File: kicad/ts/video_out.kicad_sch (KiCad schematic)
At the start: 36 parts, among them T1 PN2222A, X5 74LS157, X6 74LS157

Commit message: update footprints
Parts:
- F3, F6: footprint (none) -> Package_DIP:DIP-20_W7.62mm
- F4, X5, X6: footprint (none) -> Package_DIP:DIP-16_W7.62mm
- G2, G8: footprint (none) -> Package_DIP:DIP-14_W7.62mm
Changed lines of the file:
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@@
 			)
 		)
-		(property "Footprint" ""
+		(property "Footprint" "Package_DIP:DIP-16_W7.62mm"
 			(at 52.07 122.555 0)
 			(effects
@@
 			)
 		)
-		(property "Footprint" ""
+		(property "Footprint" "Package_DIP:DIP-16_W7.62mm"
 			(at 100.33 59.055 0)
 			(effects
@@
 			)
 		)
-		(property "Footprint" ""
+		(property "Footprint" "Package_DIP:DIP-16_W7.62mm"
 			(at 147.955 59.055 0)
 			(effects
@@
 			)
 		)
-		(property "Footprint" ""
+		(property "Footprint" "Package_DIP:DIP-20_W7.62mm"
 			(at 100.33 120.015 0)
 			(effects
@@
 			)
 		)
-		(property "Footprint" ""
+		(property "Footprint" "Package_DIP:DIP-14_W7.62mm"
 			(at 163.195 132.715 0)
 			(effects
@@
 			)
 		)
-		(property "Footprint" ""
+		(property "Footprint" "Package_DIP:DIP-20_W7.62mm"
 			(at 52.07 58.42 0)
 			(effects
@@
 			)
 		)
-		(property "Footprint" ""
+		(property "Footprint" "Package_DIP:DIP-14_W7.62mm"
 			(at 141.605 130.175 0)
 			(effects

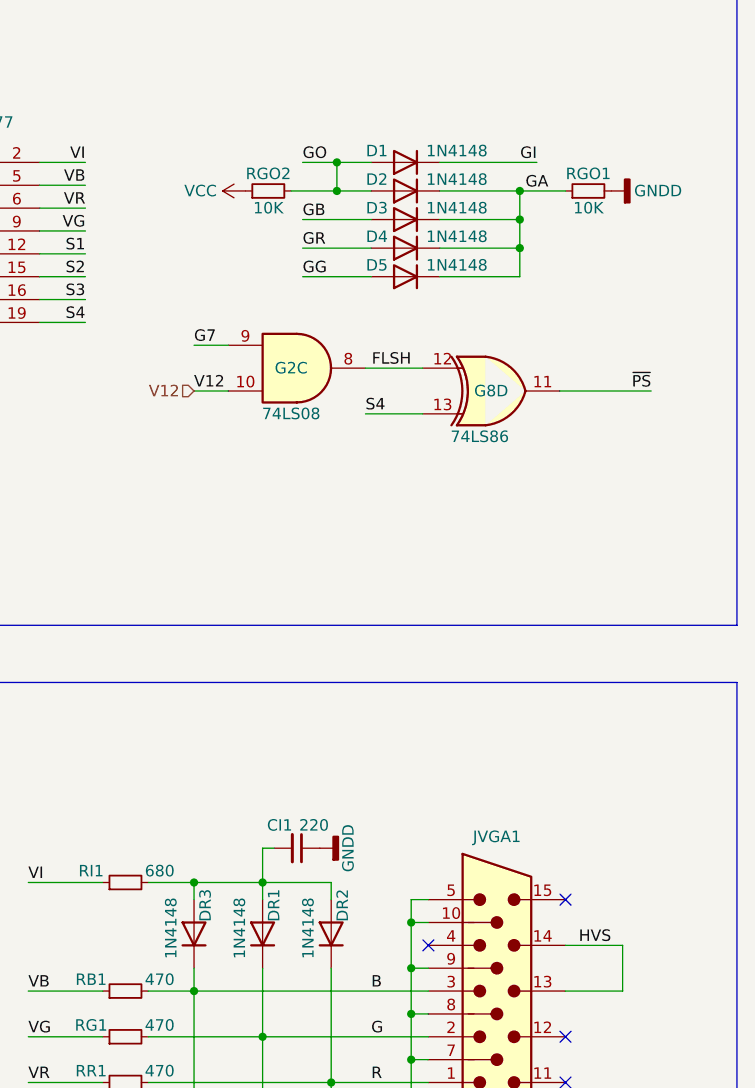
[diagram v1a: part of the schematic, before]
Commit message: Schemativ corrections, work started on pcb
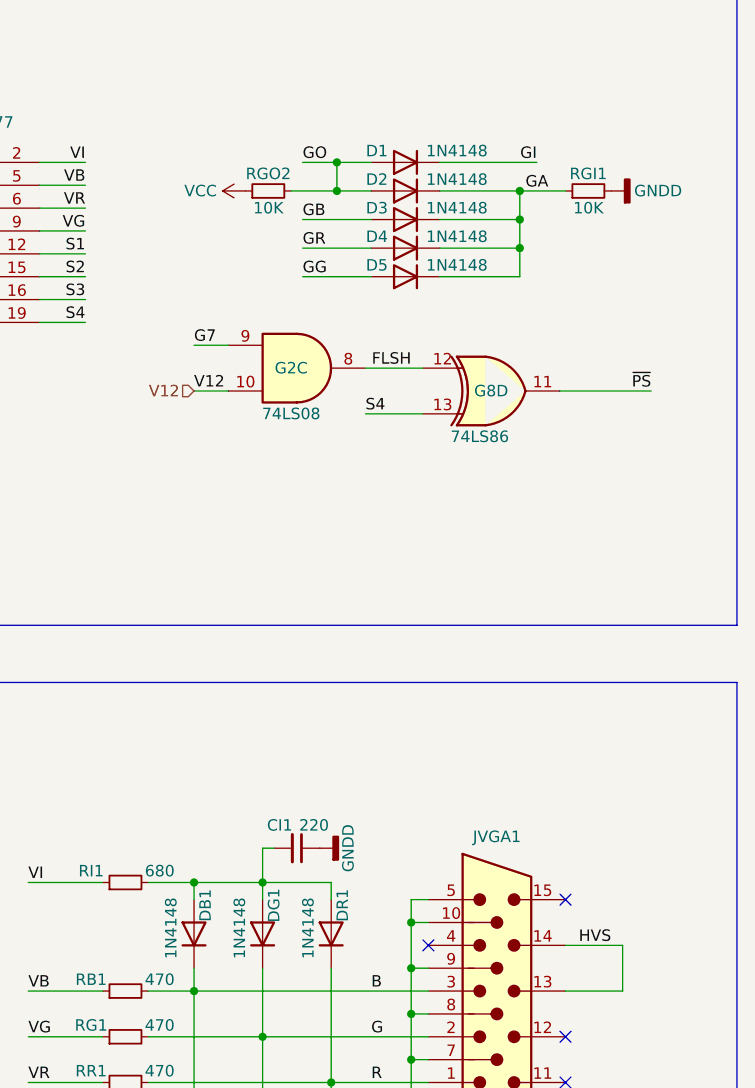
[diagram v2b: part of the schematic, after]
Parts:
- JRGBI1: footprint (none) -> Connector_Dsub:DSUB-9_Female_Horizontal_P2.77x2.84mm_EdgePinOffset7.70mm_Housed_MountingHolesOffset9.12mm
- JVGA1: footprint (none) -> Connector_Dsub:DSUB-15-HD_Female_Horizontal_P2.29x1.98mm_EdgePinOffset8.35mm_Housed_MountingHolesOffset10.89mm
- renumbered DR3 to DB1, DR1 to DG1, DR2 to DR1, RGO1 to RGI1
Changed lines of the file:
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@@
 		(on_board yes)
 		(dnp no)
-		(property "Reference" "DR1"
+		(property "Reference" "DG1"
 			(at 139.065 189.865 0)
 			(effects
@@
 			(project "ts"
 				(path "/13135b82-690b-4b84-a983-6756320cca7f/4e0c27f0-6a54-4702-a86e-449d2a0be5cf"
-					(reference "DR1")
+					(reference "DG1")
 					(unit 1)
 				)
@@
 		(on_board yes)
 		(dnp no)
-		(property "Reference" "RGO1"
+		(property "Reference" "RGI1"
 			(at 173.99 108.585 90)
 			(effects
@@
 			(project "ts"
 				(path "/13135b82-690b-4b84-a983-6756320cca7f/4e0c27f0-6a54-4702-a86e-449d2a0be5cf"
-					(reference "RGO1")
+					(reference "RGI1")
 					(unit 1)
 				)
@@
 			)
 		)
-		(property "Footprint" ""
+		(property "Footprint" "Connector_Dsub:DSUB-15-HD_Female_Horizontal_P2.29x1.98mm_EdgePinOffset8.35mm_Housed_MountingHolesOffset10.89mm"
 			(at 139.7 191.77 0)
 			(effects
@@
 		(on_board yes)
 		(dnp no)
-		(property "Reference" "DR2"
+		(property "Reference" "DR1"
 			(at 146.685 189.865 0)
 			(effects
@@
 			(project "ts"
 				(path "/13135b82-690b-4b84-a983-6756320cca7f/4e0c27f0-6a54-4702-a86e-449d2a0be5cf"
-					(reference "DR2")
+					(reference "DR1")
 					(unit 1)
 				)
@@
 		(on_board yes)
 		(dnp no)
-		(property "Reference" "DR3"
+		(property "Reference" "DB1"
 			(at 131.445 189.865 0)
 			(effects
@@
 			(project "ts"
 				(path "/13135b82-690b-4b84-a983-6756320cca7f/4e0c27f0-6a54-4702-a86e-449d2a0be5cf"
-					(reference "DR3")
+					(reference "DB1")
 					(unit 1)
 				)
@@
 			)
 		)
-		(property "Footprint" ""
+		(property "Footprint" "Connector_Dsub:DSUB-9_Female_Horizontal_P2.77x2.84mm_EdgePinOffset7.70mm_Housed_MountingHolesOffset9.12mm"
 			(at 89.535 199.39 0)
 			(effects

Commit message: Changed VGA connector to Amphenol L77HDE15SD1CH4FVGA
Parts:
- JVGA1: footprint Connector_Dsub:DSUB-15-HD_Female_Horizontal_P2.29x1.98mm_EdgePinOffset8.35mm_Housed_MountingHolesOffset10.89mm -> Cobra_original:CONN_L77HDE15SD1CH4FVGA_AMP
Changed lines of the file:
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@@
 			)
 		)
-		(property "Footprint" "Connector_Dsub:DSUB-15-HD_Female_Horizontal_P2.29x1.98mm_EdgePinOffset8.35mm_Housed_MountingHolesOffset10.89mm"
+		(property "Footprint" "Cobra_original:CONN_L77HDE15SD1CH4FVGA_AMP"
 			(at 139.7 191.77 0)
 			(effects
@@
 			)
 		)
-		(property "Datasheet" "~"
+		(property "Datasheet" "https://cdn.amphenol-cs.com/media/wysiwyg/files/drawing/l77hde15sd1ch4fvga.pdf"
 			(at 139.7 191.77 0)
 			(effects
@@
 			)
 		)
-		(property "Description" "15-pin male plug socket D-SUB connector, High density (3 columns), Triple Row, Generic, VGA-connector, Mounting Hole"
+		(property "Description" "15-pin male plug socket D-SUB connector, L77HDE15SD1CH4FVGA on Mouser"
 			(at 163.83 201.93 0)
 			(effects
